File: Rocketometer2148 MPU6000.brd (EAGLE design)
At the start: 55.9 x 22.9 mm, 76 parts, among them J001 USB_MICROB_JST, J301 JST 2mm, J401 M06, J402 M06, J701 MICROSD-SOCKET, Q050 PMOS, Q201 PMOS, U101 BMP180, U201 5319, U301 73831, U401 LPC2148, U402 SN74LVC1G32, U501 L3G4200D, U801 5883, U901 LIS331, U902 AD377, Y401 12MHz, Y402 32kiHz

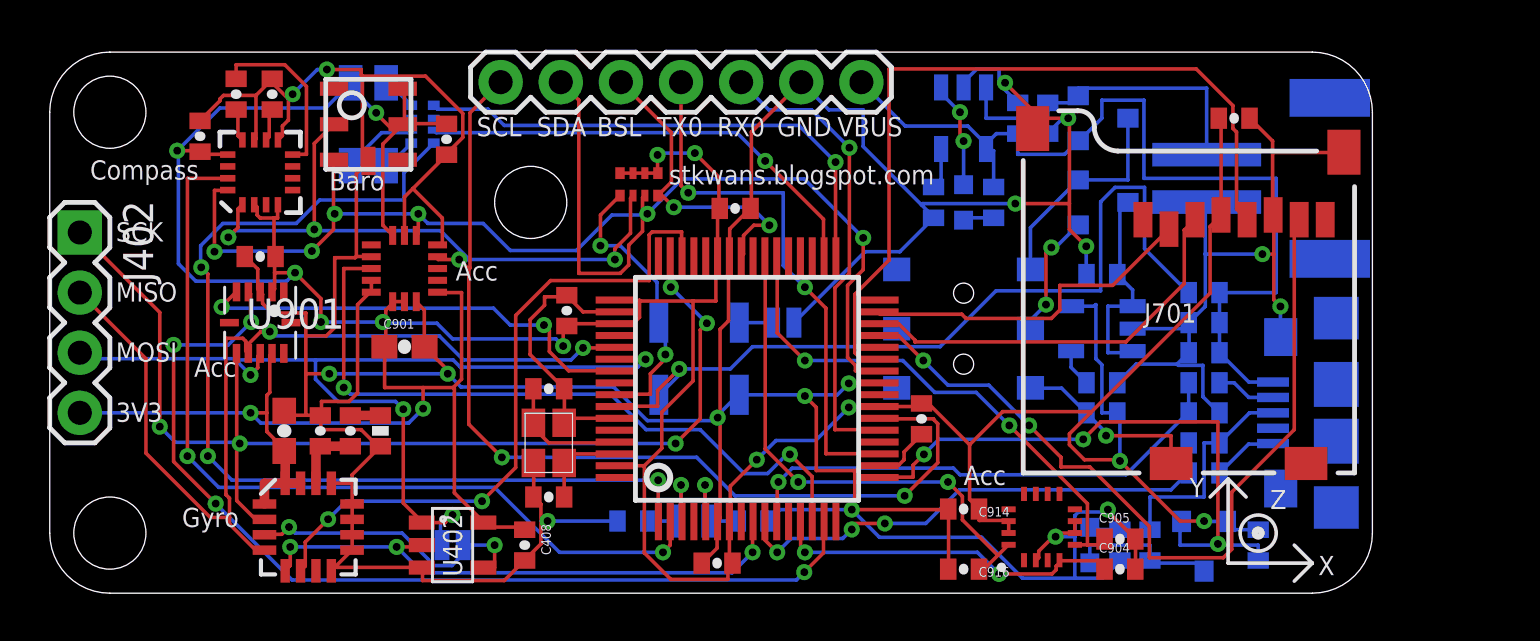
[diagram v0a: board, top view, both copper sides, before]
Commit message: Made 11DoF for BMA180, MPU6000, replaced ADXL345 with BMA180 in Rocketometer2148, made Rocketometer2148 with MPU6000
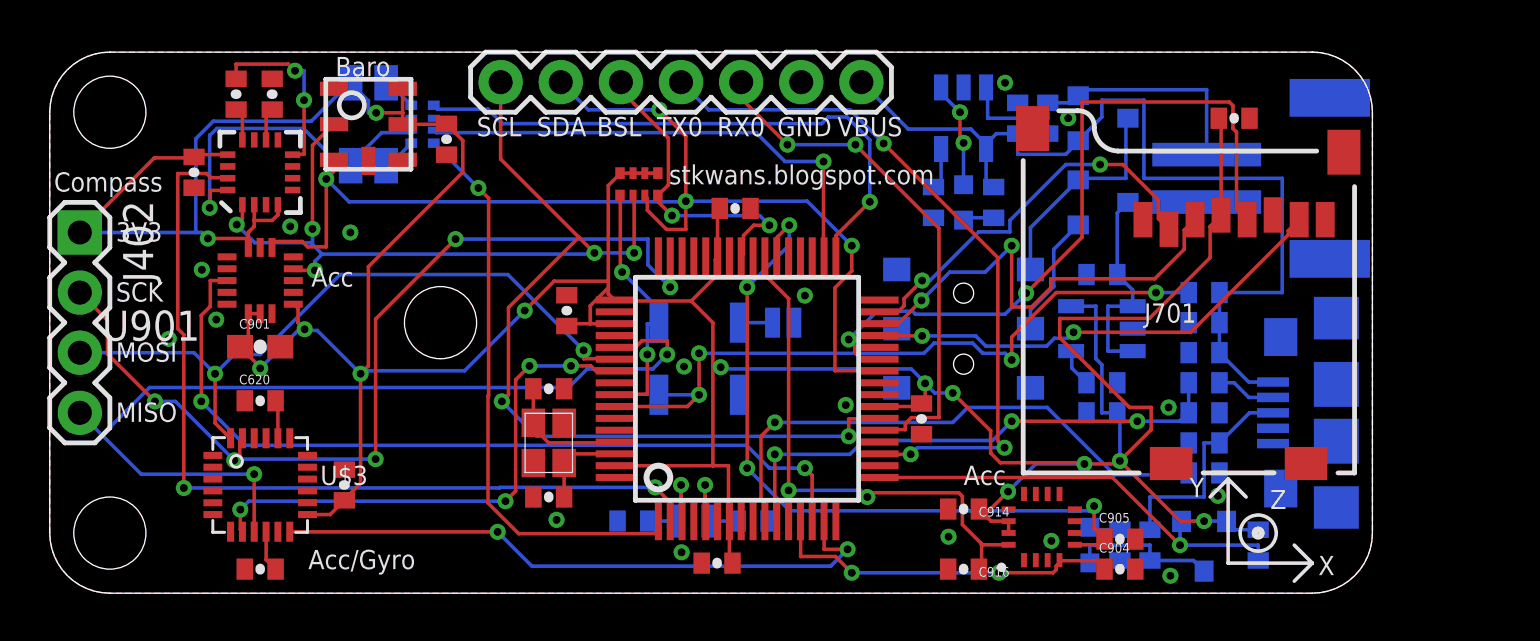
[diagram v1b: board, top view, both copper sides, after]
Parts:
- removed C408, C602: 100nF, SparkFun:0402-CAP
- removed C502: 10uF, SparkFun:0603-CAP
- removed C503: 10nF, SparkFun:0402-CAP
- removed C504: 470nF, SparkFun:0402-CAP
- removed R501: 10k, SparkFun:0402-RES
- removed S402: SOLDERJUMPERNO, SparkFun-Passives:SJ_2S-NO
- removed U402: SN74LVC1G32, KwanSystems:SOT-23-5
- removed U501: L3G4200D, SparkFun:LGA16-4X4
- added C610, C613: 100nF, SparkFun:0402-CAP
- added C620: 2.2nF, SparkFun:0402-CAP
- U$3: value BMA180 -> MPU6000; device SparkFun-Sensors:LGA12 -> KwanSystems:MPU60X0
- moved U$3 6.86 mm to (8.89, 4.57), turned to 0 degrees
- moved JP3 6.35 mm to (16.5, 11.4)
- moved U901 6.12 mm to (8.89, 13.2)
- moved C901 6.10 mm to (8.89, 10.4)
- moved U$1 2.30 mm to (15.5, 4.83)
- moved C802 1.55 mm to (6.10, 17.8), turned to 270 degrees
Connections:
- removed net CSG: U401.9, U402.2, U501.5
- removed net GMOSI1: S402.2, U402.4, U501.3
- removed net GYROINT: U401.46, U501.6
- removed net N$20: C503.1, C504.1, U501.14
- new net N$13: C610.1, U$3.10
- net ACCINT: now also U$3.12; no longer U$3.4
- net CSA: now also U$3.8; no longer U$3.5
- net GND: now also C610.2, C613.1, C620.1, U$3.1, U$3.11, U$3.18; no longer C408.2, C502.2, C503.2, C602.2, R501.1, U$3.3, U402.3, U501.10, U501.11, U501.12, U501.13, U501.8, U501.9
- net MISO1: now also J402.4, U$3.9; no longer J402.2, U$3.8, U501.4
- net MOSI1: now also U$3.24; no longer S402.1, U$3.9, U402.1
- net N$1: now also C620.2, U$3.20; no longer C504.2, R501.2
- net SCK1: now also J402.2, U$3.23; no longer J402.1, U$3.7, U501.2
- net VCC: now also C613.2, J402.1, U$3.13; no longer C408.1, C502.1, C602.1, J402.4, U$3.10, U$3.2, U402.5, U501.1, U501.15, U501.16
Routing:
- net GND: track 275.6 -> 0.00 mm, vias 18 -> 17
- net GYROINT: track 28.6 -> 0.00 mm, vias 2 -> 0
- net CSG: track 23.9 -> 0.00 mm, vias 3 -> 0
- net PWMR: track 42.5 -> 24.4 mm, vias 3 -> 1
- net MISO0: track 35.0 -> 20.2 mm
- net VCC: track 196.6 -> 181.9 mm, vias 14 -> 13
- net ACCINT: track 41.3 -> 26.6 mm, vias 4 -> 2
- net GMOSI1: track 12.8 -> 0.00 mm, vias 2 -> 0
- net MOSI1: track 40.8 -> 29.4 mm, vias 4 -> 2
- net SCK1: track 48.6 -> 39.9 mm
- net XACC: track 22.4 -> 30.9 mm, vias 2 -> 4
- net TX0: track 22.9 -> 30.0 mm, vias 2 -> 3
- net USB_LIGHT: track 25.8 -> 18.9 mm, vias 3 -> 1
- net SCL0: track 69.3 -> 62.4 mm, vias 6 -> 7
- net USB_ON: track 35.5 -> 30.1 mm, vias 1 -> 4
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- added copper zone on layer 1, net GND
- added copper zone on layer 16, net GND
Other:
- board text added: "Acc/Gyro"
- board text removed: "Gyro"

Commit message: Split off hardware stack initialization and checking
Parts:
- removed C201, C914: 4.7uF, SparkFun:0402-CAP
- removed C203, C904, C905, C916: 100nF, SparkFun:0402-CAP
- removed Q201: PMOS, SparkFun:SOT23-3
- removed U902: AD377, KwanSystems:ADXL377
- added C214, C449, C463: 100nF, SparkFun:0402-CAP
- added C215: 4.7uF, SparkFun:0402-CAP
- J401: device SparkFun-Connectors:1X07 -> SparkFun-Connectors:1X08_LOCK
- J402: device SparkFun-Connectors:1X04 -> SparkFun-Connectors:1X04_LOCK
- moved C204 7.88 mm to (44.7, 5.59), turned to 180 degrees
- moved D302 6.10 mm to (44.2, 14.0), turned to 270 degrees
- moved R301 5.64 mm to (40.6, 21.1), turned to 180 degrees
- moved U301 5.59 mm to (44.2, 19.8), turned to 270 degrees
- moved C301 4.32 mm to (44.2, 16.3), turned to 180 degrees
- moved C302 4.17 mm to (44.2, 17.5), turned to 180 degrees
- moved D301 3.88 mm to (40.6, 19.8), turned to 90 degrees
- moved U201 3.31 mm to (44.7, 7.87), turned to 90 degrees
- moved J401 2.54 mm to (36.8, 21.6)
- moved R302 2.17 mm to (40.6, 18.5), turned to 180 degrees
- moved D050 1.27 mm to (45.2, 2.03)
- moved R050 1.27 mm to (43.9, 2.03)
- moved C451 1.08 mm to (21.1, 11.2), turned to 180 degrees
- moved C901 1.02 mm to (8.89, 9.40)
- moved U901 1.02 mm to (8.89, 12.2)
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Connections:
- removed net RAW: C204.1, Q201.3, U201.1, U201.3
- removed net XACC: C905.1, U401.38, U902.5
- removed net YACC: C904.1, U401.13, U902.4
- removed net ZACC: C916.1, U401.39, U902.16
- net BSL: now also J401.6; no longer J401.5
- net GND: now also C214.2, C215.2, C449.1, C463.2, J401.3, S201.3; no longer C201.2, C203.2, C904.2, C905.2, C914.2, C916.2, J401.2, S201.1, U902.2, U902.6, U902.7
- net N$10: now also U201.3; no longer Q201.1
- net N$17: now also C214.1; no longer C203.1
- net RX0: now also J401.4; no longer J401.3
- net SCL0: now also J401.8; no longer J401.7
- net SDA0: now also J401.7; no longer J401.6
- net TX0: now also J401.5; no longer J401.4
- net VBUS: now also J401.2; no longer J401.1
- net VCC: now also C215.1, C463.1; no longer C201.1, C914.1, U401.49, U902.14, U902.15
- net VIN: now also C204.1, S201.1, U201.1; no longer Q201.2, S201.3
- net VLIPO: now also C449.2, J401.1, U401.49
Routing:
- net GND: track 0.00 -> 227.6 mm, vias 17 -> 12
- net VLIPO: track 14.4 -> 50.7 mm, vias 0 -> 7
- net XACC: track 30.9 -> 0.00 mm, vias 4 -> 0
- net ZACC: track 22.7 -> 0.00 mm, vias 2 -> 0
- net VCC: track 181.9 -> 199.9 mm, vias 13 -> 3
- net SDA0: track 61.3 -> 44.3 mm, vias 5 -> 6
- net YACC: track 15.4 -> 0.00 mm, vias 2 -> 0
- net SCL0: track 62.4 -> 49.6 mm, vias 7 -> 4
- net VBUS: track 39.7 -> 29.4 mm
- net MISO1: track 39.1 -> 28.9 mm
- net TX0: track 30.0 -> 21.2 mm
- net RAW: track 8.83 -> 0.00 mm
- net PWMB: track 21.0 -> 29.3 mm
- net SCK1: track 39.9 -> 34.9 mm, vias 5 -> 2
- net PWMG: track 24.8 -> 20.1 mm, vias 1 -> 3
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- removed copper zone on layer 1, net GND
- removed copper zone on layer 16, net GND

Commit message: Finished routing of board
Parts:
- removed C901: 10uF, SparkFun:0603-CAP
- removed U901: LIS331, KwanSystems:LLGA16
- added C904, C905, C916: 100nF, SparkFun:0402-CAP
- added C914: 4.7uF, SparkFun:0402-CAP
- added JP4, JP5: STAND-OFFTIGHT, SparkFun-Electromechanical:STAND-OFF-TIGHT
- added U902: AD377, KwanSystems:ADXL377
- moved U$2 14.2 mm to (17.8, 7.37), turned to 0 degrees
- moved R050 14.1 mm to (49.5, 15.0), turned to 0 degrees
- moved D050 12.5 mm to (49.5, 13.7), turned to 90 degrees
- moved R031 10.9 mm to (49.5, 12.4), turned to 180 degrees
- moved C030 10.8 mm to (54.1, 14.5), flipped to the top, turned to 0 degrees
- moved R030 8.69 mm to (54.1, 13.2), flipped to the top, turned to 0 degrees
- moved Q050 8.16 mm to (49.5, 10.2), turned to 270 degrees
- moved J301 7.94 mm to (57.7, 11.4)
- moved R010 7.91 mm to (54.1, 6.86), flipped to the top, turned to 0 degrees
- moved C020 6.86 mm to (54.1, 11.9), flipped to the top, turned to 0 degrees
- moved J001 6.35 mm to (59.4, 11.4), flipped to the top, turned to 90 degrees
- moved C010 6.27 mm to (54.1, 8.13), flipped to the top, turned to 180 degrees
- moved R051 6.04 mm to (49.5, 7.87), turned to 0 degrees
- moved U$1 5.85 mm to (9.65, 4.57), turned to 0 degrees
- moved R020 5.62 mm to (54.1, 10.7), flipped to the top, turned to 0 degrees
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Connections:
- new net XACC: C905.1, U401.38, U902.5
- new net YACC: C904.1, U401.13, U902.4
- new net ZACC: C916.1, U401.39, U902.16
- net GND: now also C904.2, C905.2, C914.2, C916.2, U902.2, U902.6, U902.7; no longer C901.2, U901.10, U901.12, U901.13, U901.16, U901.5, U901.7
- net HACCINT: no longer U901.11
- net SCL0: no longer U901.4
- net SDA0: no longer U901.6
- net VCC: now also C914.1, U902.14, U902.15; no longer C901.1, U901.1, U901.14, U901.15, U901.8
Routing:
- net GND: track 227.6 -> 0.00 mm, vias 12 -> 9
- net VCC: track 199.9 -> 158.8 mm, vias 3 -> 14
- net VLIPO: track 50.7 -> 85.9 mm, vias 7 -> 4
- net HACCINT: track 33.2 -> 0.00 mm, vias 4 -> 0
- net ZACC: track 0.00 -> 33.0 mm, vias 0 -> 4
- net XACC: track 0.00 -> 28.9 mm, vias 0 -> 2
- net YACC: track 0.00 -> 28.1 mm, vias 0 -> 2
- net BSL: track 13.3 -> 29.1 mm, vias 2 -> 1
- net VBUS: track 29.4 -> 44.4 mm, vias 0 -> 1
- net COMPINT: track 38.3 -> 50.4 mm, vias 4 -> 2
- net MISO1: track 28.9 -> 39.3 mm, vias 2 -> 4
- net USBD+: track 21.3 -> 30.1 mm, vias 1 -> 2
- net PWMB: track 29.3 -> 21.0 mm, vias 1 -> 3
- net SDA0: track 44.3 -> 52.1 mm
- net SCK0: track 26.9 -> 19.1 mm, vias 2 -> 0
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- added copper zone on layer 1, net GND
- added copper zone on layer 16, net GND
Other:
- board size 55.9 x 22.9 mm -> 61 x 22.9 mm
- board text added: "25 Dec 2012"
- board text added: "Boot"
- board text added: "Reset"
- board text added: "VLI"
- board text removed: "v1.0 25 Dec 2012"

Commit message: Further cleanup of board
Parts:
- U801: value 5883 -> HMC5883L
- U902: value AD377 -> ADXL377
- moved C802 1.55 mm to (6.35, 19.3), turned to 90 degrees
- moved R302 0.25 mm to (40.6, 18.3)
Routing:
- net VBUS: track 44.4 -> 47.1 mm
- net CONN_D+: track 11.3 -> 10.0 mm
- net VCC: track 158.8 -> 159.9 mm, vias 14 -> 13
- net VLIPO: track 85.9 -> 87.0 mm
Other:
- board text added: "VLIPO"

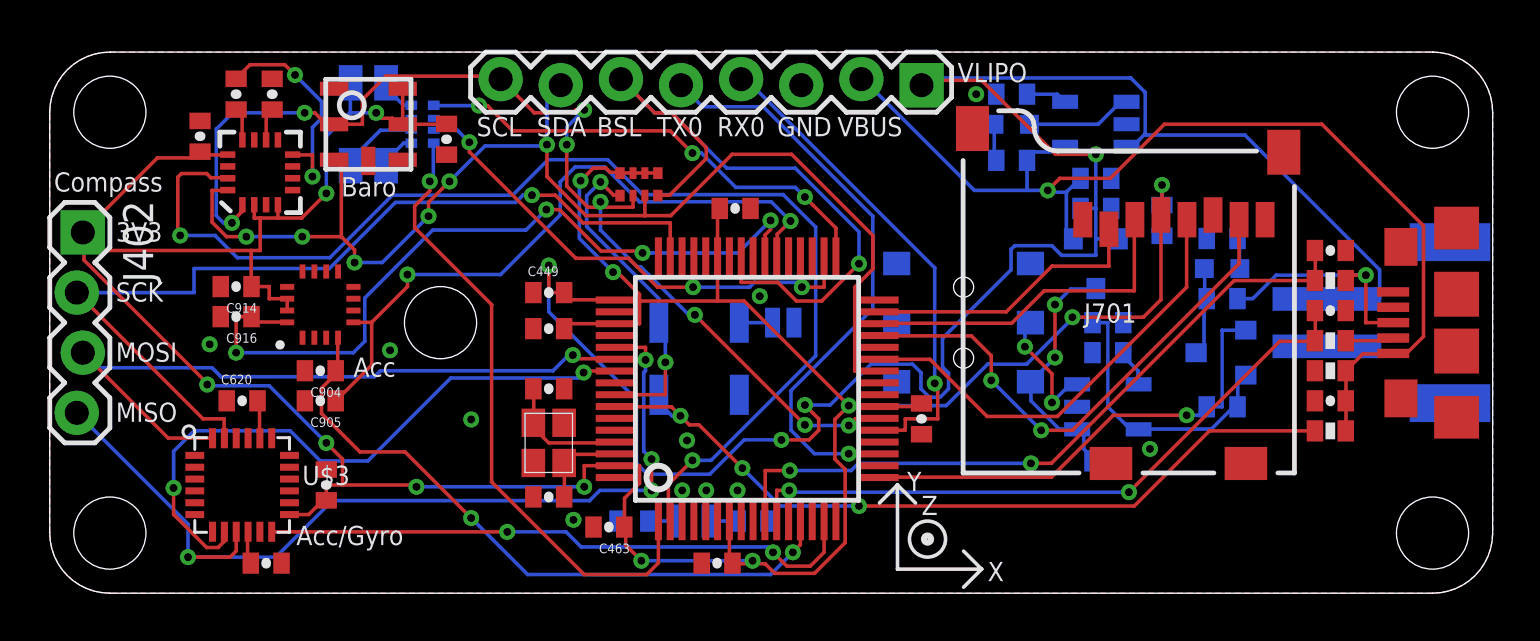
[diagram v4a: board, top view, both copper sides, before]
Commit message: Flip card slot to opposite side of board, shorten board
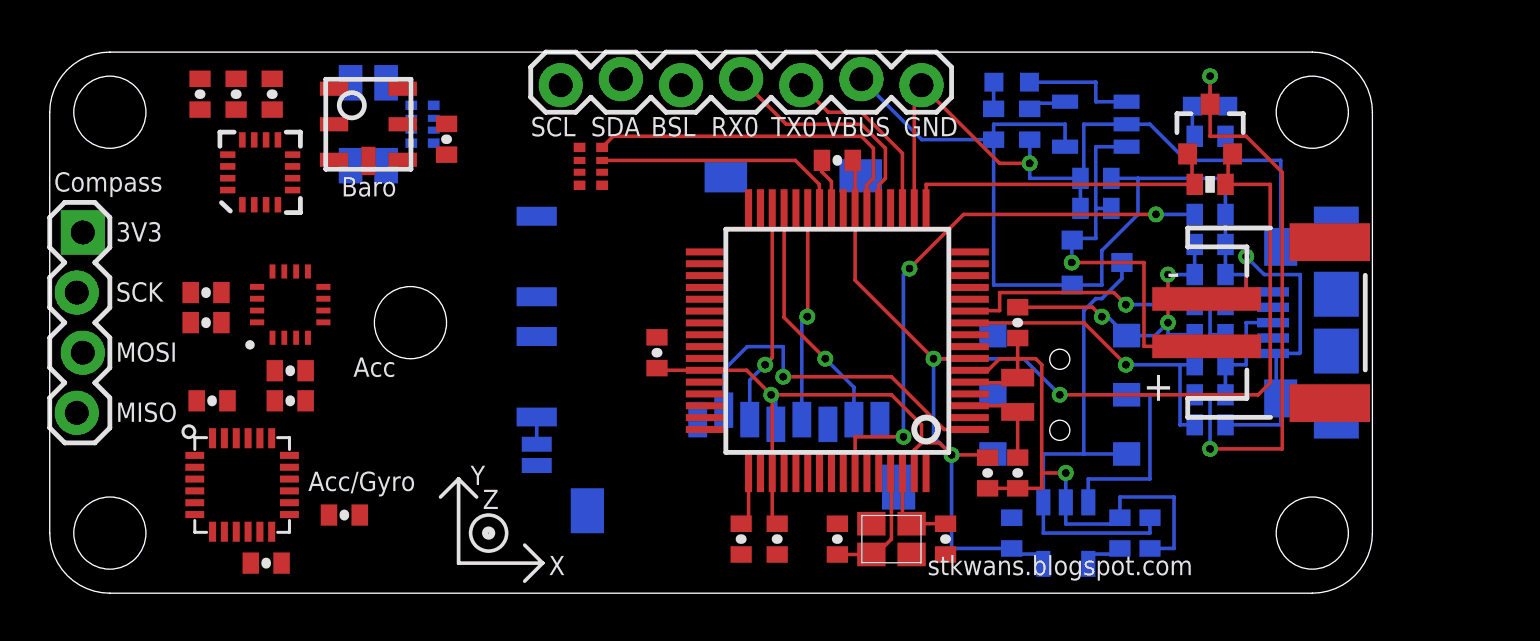
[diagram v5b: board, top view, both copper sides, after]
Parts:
- removed C463, C701: 100nF, SparkFun:0402-CAP
- added U$4: (no value), KwanSystems:AXES
- C407, C423: value 100nF -> 1uF
- J401: device SparkFun-Connectors:1X08_LOCK -> SparkFun-Connectors:1X07_LOCK
- moved J701 20.8 mm to (36.3, 18.0), flipped to the bottom, turned to 180 degrees
- moved C462 16.9 mm to (37.8, 2.29), turned to 90 degrees
- moved C403 16.4 mm to (40.9, 5.08), flipped to the top, turned to 90 degrees
- moved Y401 15.0 mm to (35.6, 2.29), turned to 0 degrees
- moved Y402 14.7 mm to (40.9, 8.38), flipped to the top, turned to 270 degrees
- moved C405 14.0 mm to (40.9, 11.4), flipped to the top, turned to 90 degrees
- moved C461 13.7 mm to (33.3, 2.29), turned to 270 degrees
- moved U$2 13.7 mm to (8.89, 17.8)
- moved C449 13.2 mm to (29.2, 2.29), turned to 90 degrees
- moved C451 13.1 mm to (30.7, 2.29), turned to 270 degrees
- moved C407 12.0 mm to (39.6, 5.08), turned to 270 degrees
- moved S457A 11.8 mm to (20.6, 5.84), turned to 270 degrees
- moved C423 11.5 mm to (33.3, 18.3), turned to 180 degrees
- moved R010 10.5 mm to (49.0, 16.0), flipped to the bottom, turned to 180 degrees
- moved C215 9.77 mm to (40.6, 2.54), turned to 90 degrees
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- renumbered U$3 to U601
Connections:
- net N$10 renamed PWR_EN
- net ACCINT: now also U401.46; no longer U401.15
- net BSL: now also J401.5, R401.1; no longer J401.6, R401.4
- net CS0: now also U401.1; no longer U401.31
- net CSA: now also U401.37; no longer U401.55
- net GND: now also J401.1; no longer C463.2, C701.2, J401.3
- net PWMR: now also U401.31; no longer U401.1
- net RESET: now also R401.2; no longer R401.1
- net SCL0: now also J401.7, R401.4; no longer J401.8, R401.2
- net SDA0: now also J401.6; no longer J401.7
- net TX0: now also J401.3; no longer J401.5
- net VCC: no longer C463.1, C701.1
- net VLIPO: no longer J401.1
- net YACC: now also U401.45; no longer U401.13
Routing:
- net GND: track 0.00 -> 88.6 mm, vias 9 -> 6
- net VCC: track 159.9 -> 75.6 mm, vias 13 -> 4
- net VLIPO: track 87.0 -> 19.5 mm, vias 4 -> 1
- net COMPINT: track 50.4 -> 0.00 mm, vias 2 -> 0
- net SDA0: track 52.1 -> 10.6 mm, vias 6 -> 0
- net MISO1: track 39.3 -> 0.00 mm, vias 4 -> 0
- net SCK1: track 38.5 -> 0.00 mm, vias 1 -> 0
- net SCL0: track 47.5 -> 14.5 mm, vias 8 -> 0
- net ZACC: track 33.0 -> 0.00 mm, vias 4 -> 0
- net MOSI1: track 30.3 -> 0.00 mm, vias 1 -> 0
- net BSL: track 29.1 -> 0.00 mm, vias 1 -> 0
- net XACC: track 28.9 -> 0.00 mm, vias 2 -> 0
- net YACC: track 28.1 -> 0.00 mm, vias 2 -> 0
- net CSA: track 27.0 -> 0.00 mm, vias 2 -> 0
- net PWMR: track 26.6 -> 0.00 mm, vias 1 -> 0
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- removed copper zone on layer 1, net GND
- removed copper zone on layer 16, net GND
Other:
- board size 61 x 22.9 mm -> 55.9 x 22.9 mm
- board text added: "v1.0 25 Dec 2012"
- board text removed: "25 Dec 2012"
- board text removed: "G"
- board text removed: "S"
- board text removed: "VLI"
- board text removed: "VLIPO"
- board text removed: "X"
- board text removed: "Y"
- board text removed: "Z"
